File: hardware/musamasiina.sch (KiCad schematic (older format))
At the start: 31 parts

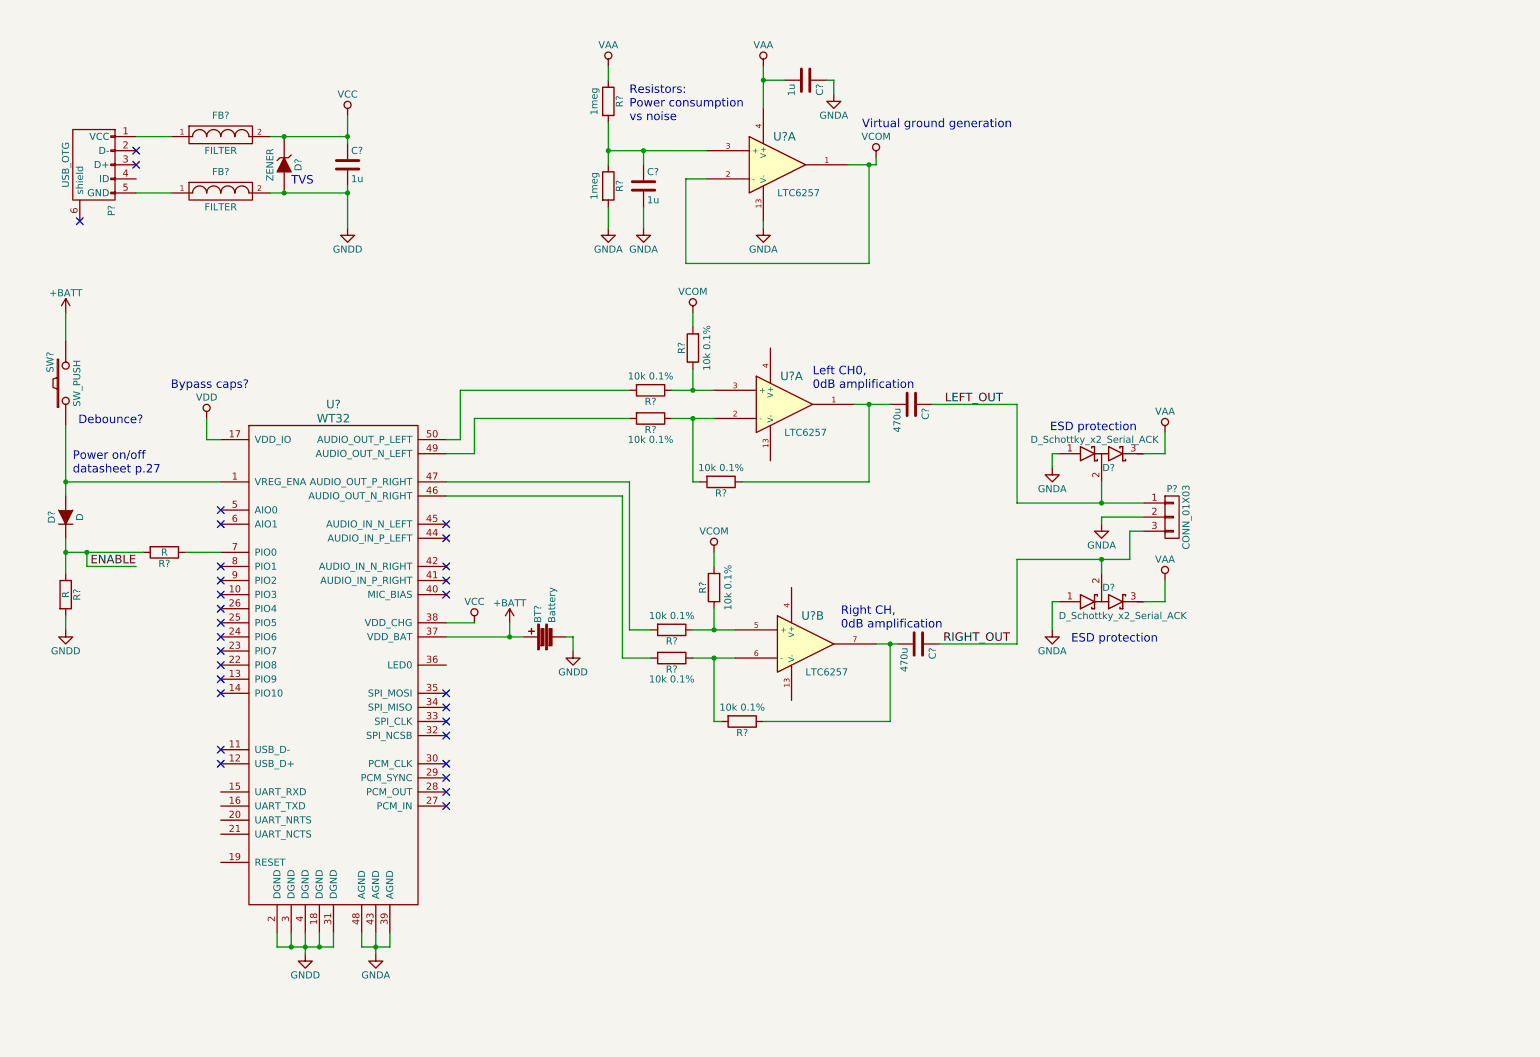
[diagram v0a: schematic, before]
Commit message: Start vorking on PSU
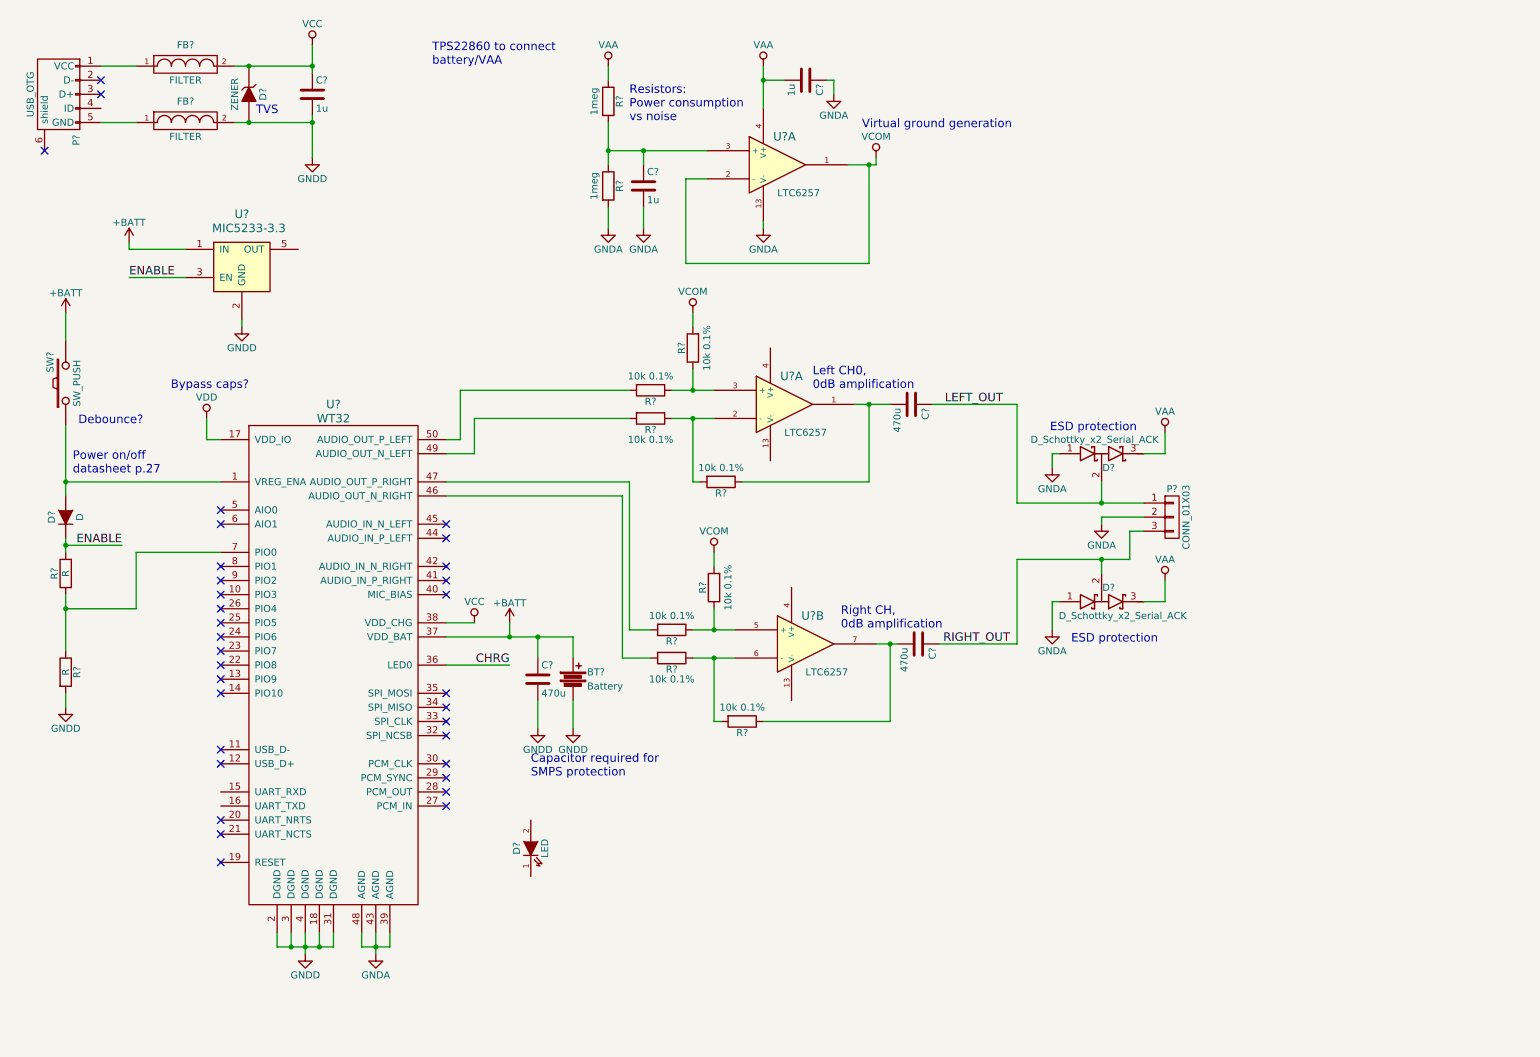
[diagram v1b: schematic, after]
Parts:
- added C?: 470u, symbol C
- added D?: LED, symbol LED
- added U?: MIC5233-3.3, symbol MIC5233-xx
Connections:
- net +BATT: now also C?.1, U?.1 (IN)
- net ENABLE: now also U?.3 (EN); no longer R?.1
- net GNDD: now also C?.2, U?.2 (GND)
- net CHRG: now reaches U?.36 (LED0)
- net at R?.1, U?.7 (PIO0): now also R?.1
- no-connect marks 30 -> 33
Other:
- note added: "Capacitor required for \nSMPS protection"
- note added: "TPS22860 to connect \nbattery/VAA"
- moved on the sheet: BT?, C?, D?, FB?, P?, R?

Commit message: Schematic ready for review
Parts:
- added 15k1, 18k1: R, symbol R
- added C1, C2, C3, C5, C6, C7, C8: 2u2, symbol C
- added C14, C15, C17, C18, C19, C20: 47p, symbol C
- added C16: 470u, symbol C
- added D10, D11, D8, D9: BAT54S, symbol D_Schottky_x2_Serial_ACK
- added D2: D_Schottky, symbol D_Schottky
- added D3: LED, symbol LED
- added FB3, FB4, FB5, FB6, FB7, FB8: FILTER, symbol FILTER
- added P3, P4: SJ1-352XN, symbol CONN_01X03
- added R18, R19, R20, R21, R3, R4, R7: 10k, symbol R
- added R5, R6: 10R, symbol R
- added U3: TPS22860, symbol TPS22860
- added unit 4 of U4
- BT1: renamed from BT?; value Battery -> 18650
- C10, C13, C4: renamed from C?; value 1u -> 2u2
- C9: renamed from C?; value 470u -> AFK477M10F24T-F
- D6, D7: renamed from D?; value D_Schottky_x2_Serial_ACK -> BAT54S
- P2: renamed from P?; value CONN_01X03 -> SJ1-352XN
- R1: renamed from R?; value R -> 10k
- R10, R11, R12, R13, R14, R15, R8, R9: renamed from R?; value 10k 0.1% -> 10k 1%
- R2: renamed from R?; value R -> 1meg
- gave numbers to parts that had none: 14
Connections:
- net labels added: IN_LEFT, IN_RIGHT, RXD, TXD, USB_DN, USB_DP, VESD
- wire segments 107 -> 231
- no-connect marks 33 -> 24
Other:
- note added: "1.5V for ESD\nstrike mitigation.\nCapacitor close to\nESD entry point"
- note added: "3.5mm in"
- note added: "3.5mm mono"
- note added: "3.5mm out"
- note added: "470u\n16V"
- note added: "?"
- note added: "Capacitor required for \nSMPS protection.\nDO NOT REPLACE."
- note added: "Capacitor: \nPower-on pop"
- note added: "Connect CTS, RTS\nif no flow control.\niWRAP user guide p.10"
- note added: "Integrated \nprotection\ncircuit"
- note added: "Mono output"
- note added: "NO EXTERNAL\nPULLUP/DOWN\nfor reset"
- note added: "OPTIONAL"
- note added: "Optional"
- note added: "Powered by VBATT or VUSB"
- note added: "Single-ended line input"
- note added: "Virtual ground\ngeneration"
- note added: "ext. pullup required \nfor RXD"
- note added: "total bus capacitance 4.4u"
- note removed: "Capacitor required for \nSMPS protection"
- note removed: "TPS22860 to connect \nbattery/VAA"
- note removed: "Virtual ground generation"
- moved on the sheet: BT1, C10, C11, C12, C13, C9, D1, D5, D6, D7, P2, R1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

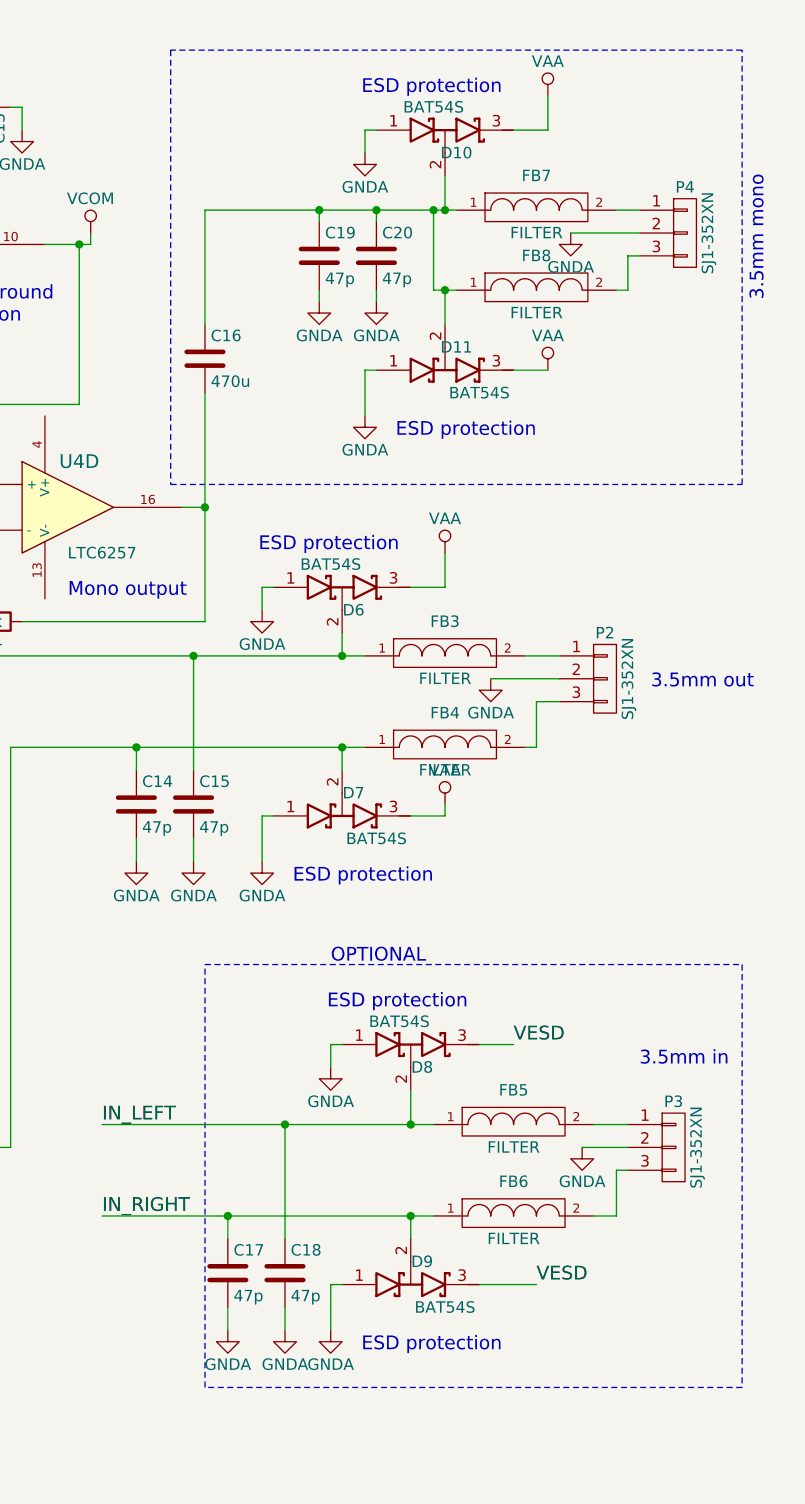
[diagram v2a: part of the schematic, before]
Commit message: Fix #2
Corrected BAT54S pin order, updated schematic
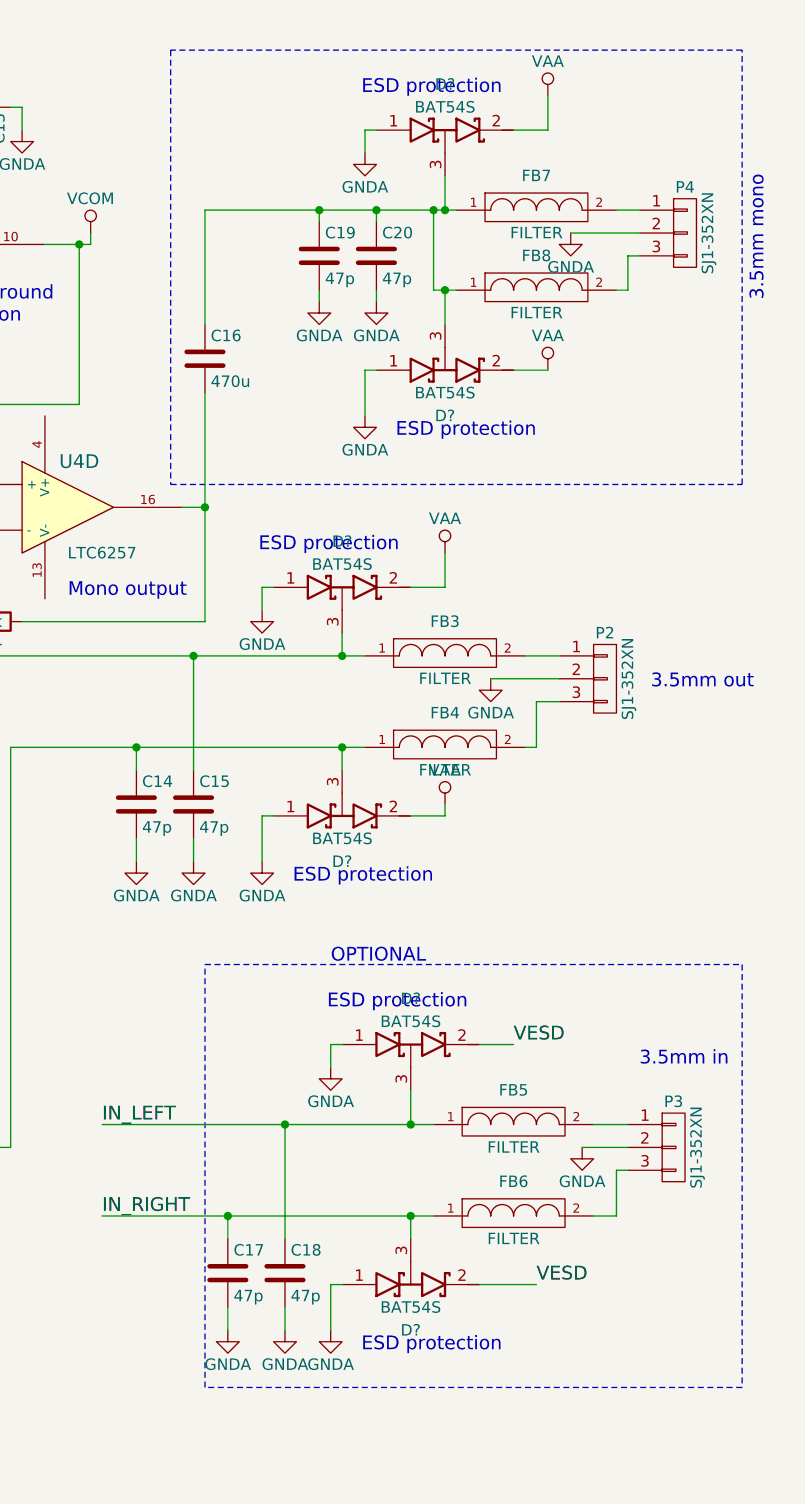
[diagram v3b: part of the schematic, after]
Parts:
- removed D10, D11, D6, D7, D8, D9: BAT54S, symbol D_Schottky_x2_Serial_ACK
- added D? (x6): BAT54S, symbol BAT54S
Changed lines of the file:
@@
 LIBS:ltc6242
 LIBS:mic5233-xx
-LIBS:tps22860
+LIBS:bat54s
 LIBS:musamasiina-cache
 EELAYER 25 0
@@
 ESD protection
 $Comp
-L D_Schottky_x2_Serial_ACK D6
-U 1 1 57392FFB
-P 9150 2950
-F 0 "D6" H 9200 2850 50  0000 C CNN
-F 1 "BAT54S" H 9100 3050 50  0000 C CNN
-F 2 "" H 9150 2950 50  0000 C CNN
-F 3 "" H 9150 2950 50  0000 C CNN
-	1    9150 2950
-	1    0    0    -1
-$EndComp
-$Comp
-L D_Schottky_x2_Serial_ACK D7
-U 1 1 57393248
-P 9150 3950
-F 0 "D7" H 9200 3850 50  0000 C CNN
-F 1 "BAT54S" H 9300 4050 50  0000 C CNN
-F 2 "" H 9150 3950 50  0000 C CNN
-F 3 "" H 9150 3950 50  0000 C CNN
-	1    9150 3950
-	1    0    0    1
-$EndComp
-$Comp
 L MIC5233-xx U1
 U 1 1 5739535D
@@
 Text Notes 9850 6300 2    60   ~ 0
 ESD protection
-$Comp
-L D_Schottky_x2_Serial_ACK D8
-U 1 1 5739DEC7
-P 9450 4950
-F 0 "D8" H 9500 4850 50  0000 C CNN
-F 1 "BAT54S" H 9400 5050 50  0000 C CNN
-F 2 "" H 9450 4950 50  0000 C CNN
-F 3 "" H 9450 4950 50  0000 C CNN
-	1    9450 4950
-	1    0    0    -1
-$EndComp
-$Comp
-L D_Schottky_x2_Serial_ACK D9
-U 1 1 5739DECD
-P 9450 6000
-F 0 "D9" H 9500 5900 50  0000 C CNN
-F 1 "BAT54S" H 9600 6100 50  0000 C CNN
-F 2 "" H 9450 6000 50  0000 C CNN
-F 3 "" H 9450 6000 50  0000 C CNN
-	1    9450 6000
-	1    0    0    1
-$EndComp
 Text Notes 10450 5050 0    60   ~ 0
 3.5mm in
@@
 Text Notes 10000 2300 2    60   ~ 0
 ESD protection
-$Comp
-L D_Schottky_x2_Serial_ACK D10
-U 1 1 573B2604
-P 9600 950
-F 0 "D10" H 9650 850 50  0000 C CNN
-F 1 "BAT54S" H 9550 1050 50  0000 C CNN
-F 2 "" H 9600 950 50  0000 C CNN
-F 3 "" H 9600 950 50  0000 C CNN
-	1    9600 950
-	1    0    0    -1
-$EndComp
-$Comp
-L D_Schottky_x2_Serial_ACK D11
-U 1 1 573B260A
-P 9600 2000
-F 0 "D11" H 9650 1900 50  0000 C CNN
-F 1 "BAT54S" H 9750 2100 50  0000 C CNN
-F 2 "" H 9600 2000 50  0000 C CNN
-F 3 "" H 9600 2000 50  0000 C CNN
-	1    9600 2000
-	1    0    0    1
-$EndComp
 Text Notes 11000 1700 1    60   ~ 0
 3.5mm mono
@@
 	1    0    0    -1
 $EndComp
+$Comp
+L BAT54S D?
+U 1 1 573F7EAE
+P 9600 950
+F 0 "D?" H 9600 1150 50  0000 C CNN
+F 1 "BAT54S" H 9600 1050 50  0000 C CNN
+F 2 "" H 9600 950 50  0000 C CNN
+F 3 "" H 9600 950 50  0000 C CNN
+	1    9600 950
+	1    0    0    -1
+$EndComp
+$Comp
+L BAT54S D?
+U 1 1 573F7F69
+P 9600 2000
+F 0 "D?" H 9600 2200 50  0000 C CNN
+F 1 "BAT54S" H 9600 2100 50  0000 C CNN
+F 2 "" H 9600 2000 50  0000 C CNN
+F 3 "" H 9600 2000 50  0000 C CNN
+	1    9600 2000
+	1    0    0    1
+$EndComp
+$Comp
+L BAT54S D?
+U 1 1 573F802E
+P 9150 2950
+F 0 "D?" H 9150 3150 50  0000 C CNN
+F 1 "BAT54S" H 9150 3050 50  0000 C CNN
+F 2 "" H 9150 2950 50  0000 C CNN
+F 3 "" H 9150 2950 50  0000 C CNN
+	1    9150 2950
+	1    0    0    -1
+$EndComp
+$Comp
+L BAT54S D?
+U 1 1 573F80FF
+P 9150 3950
+F 0 "D?" H 9150 4150 50  0000 C CNN
+F 1 "BAT54S" H 9150 4050 50  0000 C CNN
+F 2 "" H 9150 3950 50  0000 C CNN
+F 3 "" H 9150 3950 50  0000 C CNN
+	1    9150 3950
+	1    0    0    1
+$EndComp
+$Comp
+L BAT54S D?
+U 1 1 573F8794
+P 9450 4950
+F 0 "D?" H 9450 5150 50  0000 C CNN
+F 1 "BAT54S" H 9450 5050 50  0000 C CNN
+F 2 "" H 9450 4950 50  0000 C CNN
+F 3 "" H 9450 4950 50  0000 C CNN
+	1    9450 4950
+	1    0    0    -1
+$EndComp
+$Comp
+L BAT54S D?
+U 1 1 573F8863
+P 9450 6000
+F 0 "D?" H 9450 6200 50  0000 C CNN
+F 1 "BAT54S" H 9450 6100 50  0000 C CNN
+F 2 "" H 9450 6000 50  0000 C CNN
+F 3 "" H 9450 6000 50  0000 C CNN
+	1    9450 6000
+	1    0    0    1
+$EndComp
 $EndSCHEMATC

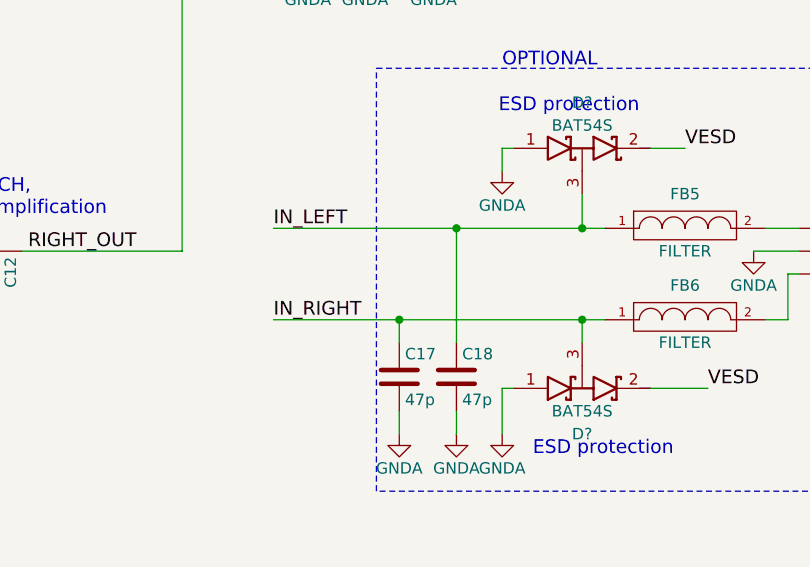
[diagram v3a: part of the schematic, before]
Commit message: Add AC-coupling caps to mic input. Fixes #4
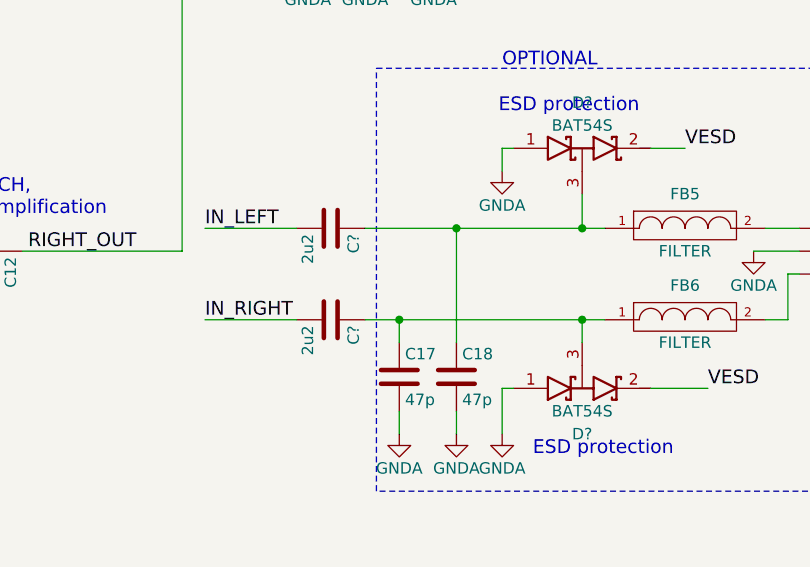
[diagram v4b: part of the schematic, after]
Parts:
- added C? (x2): 2u2, symbol C
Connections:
- wire segments 231 -> 233
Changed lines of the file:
@@
 Text Label 10000 6000 0    60   ~ 0
 VESD
-Text Label 8100 5700 0    60   ~ 0
+Text Label 7800 5700 0    60   ~ 0
 IN_RIGHT
-Text Label 8100 5300 0    60   ~ 0
+Text Label 7800 5300 0    60   ~ 0
 IN_LEFT
 Text Label 1450 950  2    60   ~ 0
@@
 	3500 4950 3900 4950
 Wire Wire Line
-	8100 5700 9550 5700
-Wire Wire Line
-	8100 5300 9550 5300
+	8500 5700 9550 5700
+Wire Wire Line
+	8500 5300 9550 5300
 Wire Wire Line
 	9450 5300 9450 5150
@@
 	1    0    0    1
 $EndComp
+$Comp
+L C C?
+U 1 1 573F922D
+P 8350 5300
+F 0 "C?" H 8375 5400 50  0000 L CNN
+F 1 "2u2" H 8375 5200 50  0000 L CNN
+F 2 "" H 8388 5150 50  0000 C CNN
+F 3 "" H 8350 5300 50  0000 C CNN
+	1    8350 5300
+	0    1    1    0
+$EndComp
+$Comp
+L C C?
+U 1 1 573F9334
+P 8350 5700
+F 0 "C?" H 8375 5800 50  0000 L CNN
+F 1 "2u2" H 8375 5600 50  0000 L CNN
+F 2 "" H 8388 5550 50  0000 C CNN
+F 3 "" H 8350 5700 50  0000 C CNN
+	1    8350 5700
+	0    1    1    0
+$EndComp
+Wire Wire Line
+	8200 5300 7800 5300
+Wire Wire Line
+	7800 5700 8200 5700
 $EndSCHEMATC

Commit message: divide schematic into subscheets
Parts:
- removed 15k1, 18k1: R, symbol R
- removed C2, C3, C4, C5, C6: 2u2, symbol C
- removed D2: D_Schottky, symbol D_Schottky
- removed D4: ZENER, symbol ZENER
- removed D5: LED, symbol LED
- removed FB1, FB2: FILTER, symbol FILTER
- removed R7: 10k, symbol R
- removed U1: MIC5233-3.3, symbol MIC5233-xx
- removed U3: TPS22860, symbol TPS22860
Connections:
- net labels added: CS, MISO, MOSI, SCLK
- wire segments 233 -> 197
- no-connect marks 24 -> 20
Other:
- note removed: "1.5V for ESD\nstrike mitigation.\nCapacitor close to\nESD entry point"
- note removed: "Powered by VBATT or VUSB"
- note removed: "TVS"
- note removed: "total bus capacitance 4.4u"
- moved on the sheet: P1
